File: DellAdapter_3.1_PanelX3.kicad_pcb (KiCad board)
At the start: 2 copper layers, 63.2 x 50.3 mm, 57 parts, among them J1 USB4065-XX-X_REVA, J2 USB4151-GF-C_REVA

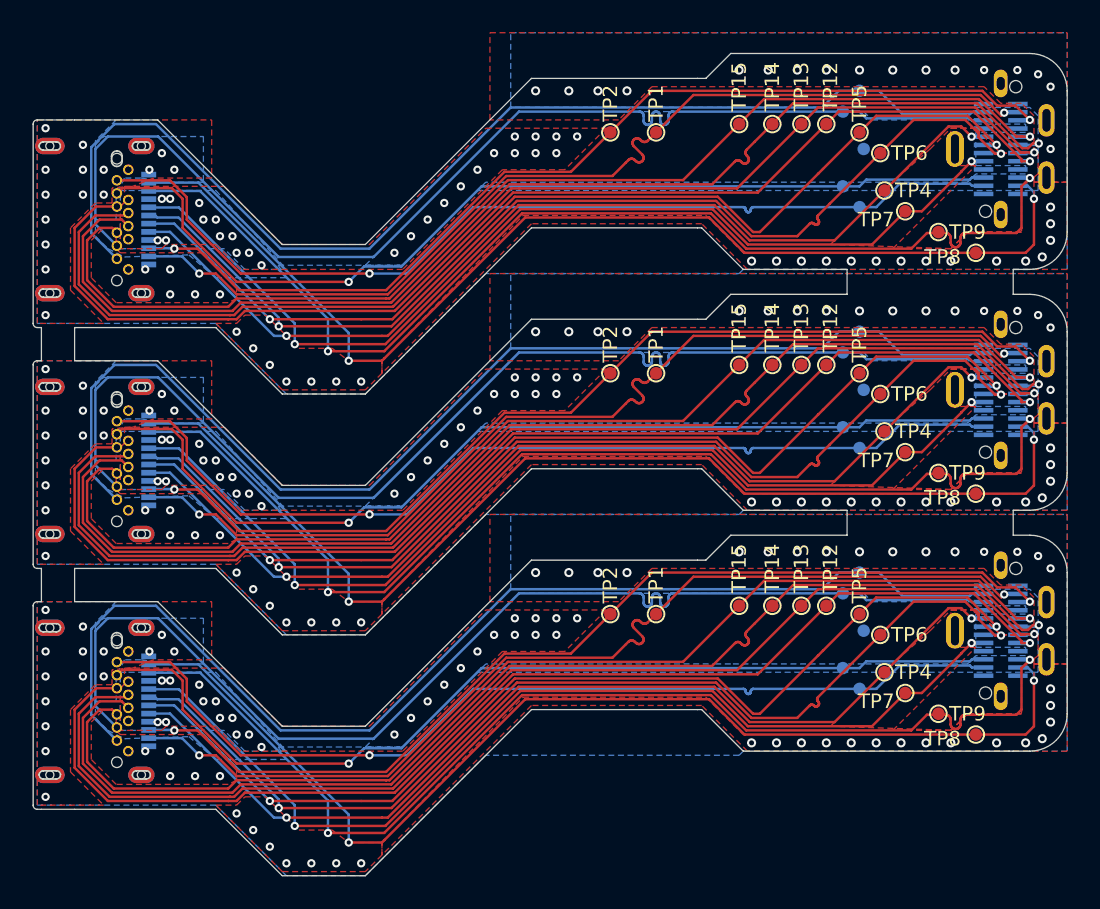
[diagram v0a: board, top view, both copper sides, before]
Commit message: shrink tolerances on footprints
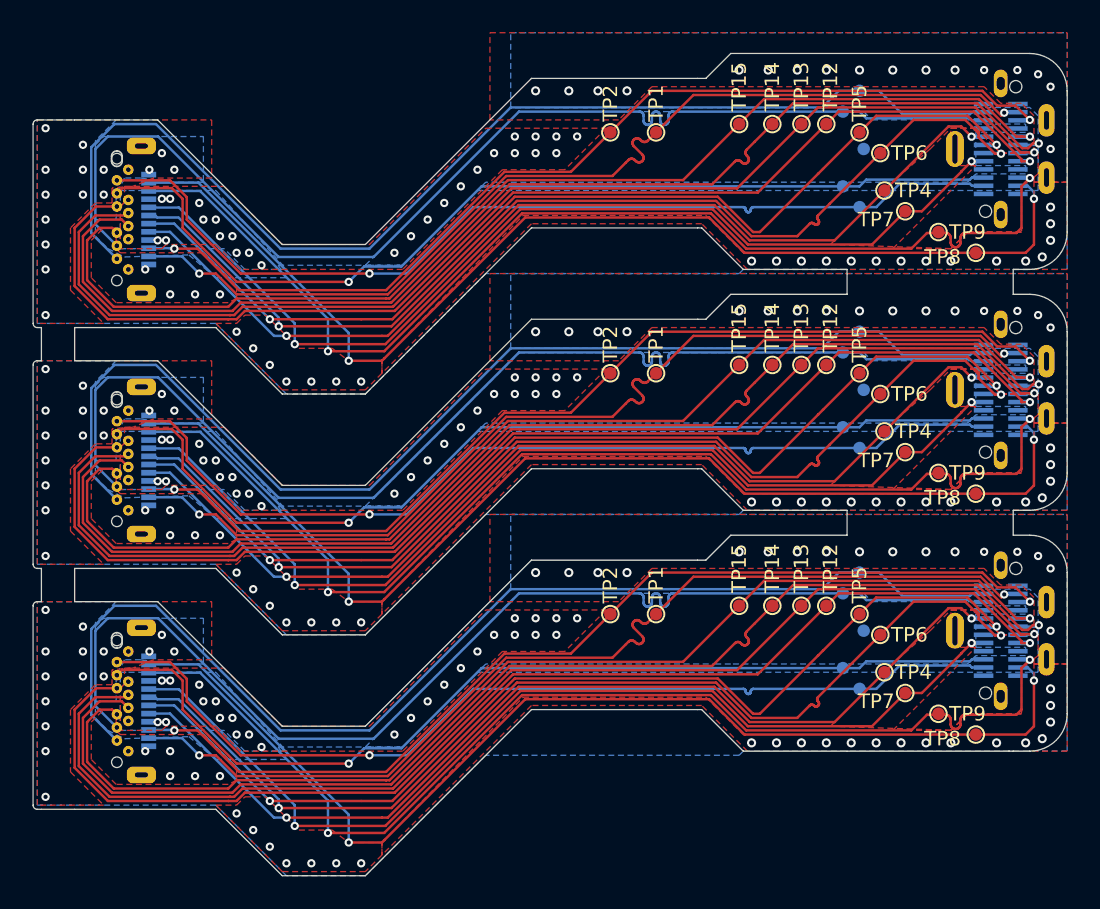
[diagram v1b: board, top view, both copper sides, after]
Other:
- rule trace_min: 0.1524 -> 0.1016
- rule via_min_size: 0.508 -> 0.3048
- board text added: "Rev. 3.3 - 14 Jan 2021"
- board text removed: "Rev. 3.2 - 5 Dec 2020"
